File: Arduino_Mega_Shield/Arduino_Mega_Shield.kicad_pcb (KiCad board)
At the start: 4 copper layers, 99.5 x 53.3 mm, 58 parts, among them J1 Conn_01x04, J11 SW6, J12 SW7, J13 SW8, J14 SW9, J15 Motor Driver Connector, J16 Motor Driver Connector, J17 Motor Driver Connector, J18 Motor Driver Connector, J19 Screw_Terminal_01x02, J2 Conn_01x04, J20 JOYSTICK, J21 I2C CONNECTOR, J22 ENCODER1, J23 ENCODER2, J24 ENCODER3, J25 ENCODER4, J26 UART CONNECTOR, J27 3_pin_selector, J28 3_pin_selector, J29 3_pin_selector, J3 Conn_01x04, J30 3_pin_selector, J31 3_pin_selector, J32 3_pin_selector, J33 3_pin_selector, J34 3_pin_selector, J35 3_pin_selector, J36 3_pin_selector, J37 3_pin_selector, J38 3_pin_selector, J39 SW10, J4 Conn_01x04, J5 SW5, J6 SW1, J7 SW2, J8 SW3, J9 SW4

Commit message: Final version of the PCB
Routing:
- net SW8: track 0.00 -> 124.6 mm, vias 0 -> 1
- net SW6: track 0.00 -> 107.0 mm, vias 0 -> 2
- net SW7: track 0.00 -> 104.2 mm, vias 0 -> 2
- net SW5: track 0.00 -> 99.0 mm, vias 0 -> 1
- net SW4: track 0.00 -> 90.1 mm, vias 0 -> 2
- net SW3: track 0.00 -> 81.7 mm, vias 0 -> 1
- net SW2: track 0.00 -> 78.4 mm
- net SW1: track 0.00 -> 71.4 mm, vias 0 -> 1
- net SW9: track 0.00 -> 30.2 mm
- net SW10: track 0.00 -> 25.9 mm, vias 0 -> 1
- net +12V: track 226.7 -> 224.8 mm
- net VRY: track 61.8 -> 60.5 mm
- net R_IS3: track 76.6 -> 77.5 mm
- net ENC_A1: track 16.8 -> 15.9 mm
- net R_IS2: track 52.5 -> 51.8 mm
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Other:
- board text added: "STAR"
- board text added: "TMB"
- board text added: "TRACK"
- board text removed: "Made by Josserand-Pierre Gay with the help of Simon Guillemette"

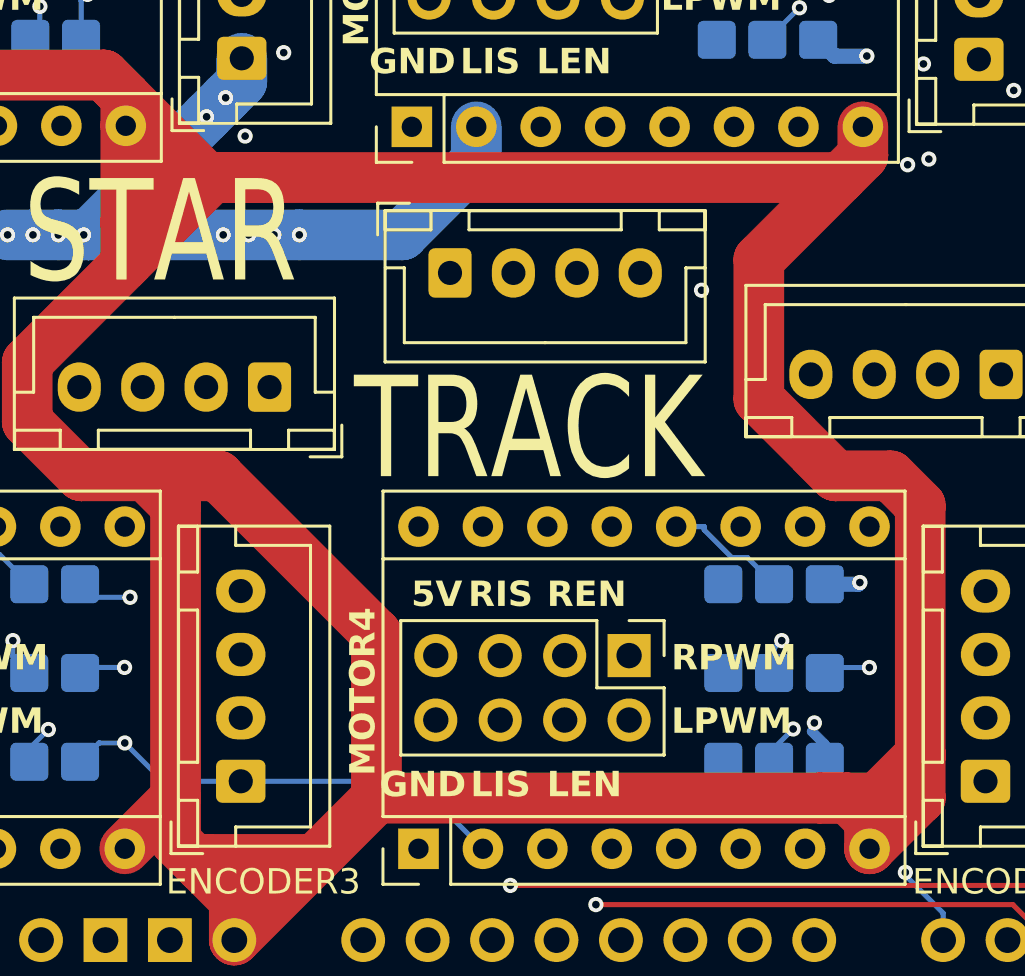
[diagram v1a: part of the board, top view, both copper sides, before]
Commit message: Refactor of the Arduino code to improve readability and debugging
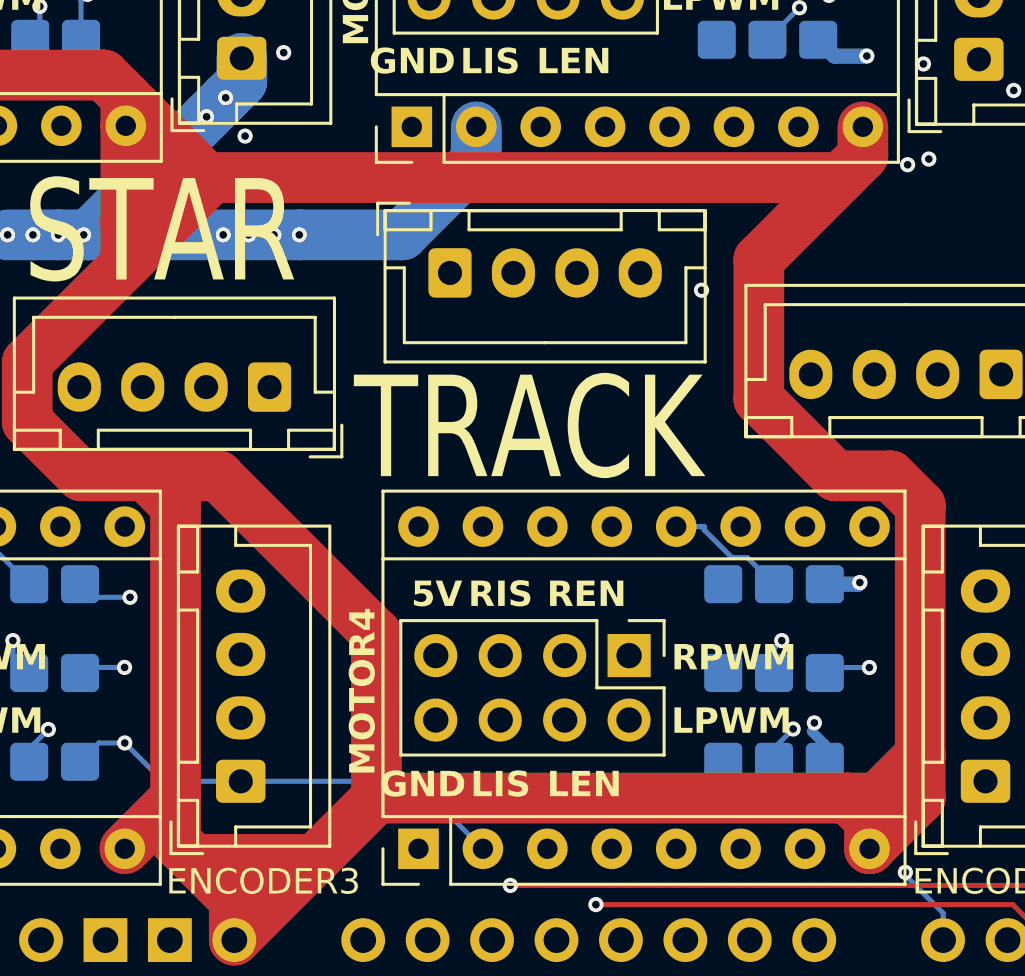
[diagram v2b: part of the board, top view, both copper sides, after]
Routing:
- net +12V: track 224.8 -> 218.1 mm
- net SW6: track 107.0 -> 105.0 mm
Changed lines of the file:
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@@
-	)
-	(segment
-		(start 139 84.241)
-		(end 138.06 84.241)
-		(width 2)
-		(layer "F.Cu")
-		(net 61)
 	)
 	(segment
@@
 	)
 	(segment
-		(start 140.5 84.241)
-		(end 139 84.241)
-		(width 2)
-		(layer "F.Cu")
-		(net 61)
-	)
-	(segment
 		(start 117.735 80.199)
 		(end 133.79 80.199)
@@
 	)
 	(segment
-		(start 137.832 84.241)
-		(end 136.701 84.241)
-		(width 2)
-		(layer "F.Cu")
-		(net 61)
-	)
-	(segment
 		(start 111.999 73.8628)
 		(end 113.939 73.8628)
@@
 	)
 	(segment
-		(start 137.832 84.241)
-		(end 138.06 84.241)
-		(width 2)
-		(layer "F.Cu")
-		(net 61)
-	)
-	(segment
 		(start 133.79 80.199)
 		(end 137.832 84.241)
@@
 	)
 	(segment
-		(start 138.06 84.241)
-		(end 139 84.241)
-		(width 2)
-		(layer "F.Cu")
-		(net 61)
-	)
-	(segment
 		(start 133.79 80.199)
 		(end 134.66 81.0686)
@@
 	)
 	(segment
-		(start 137.832 84.241)
-		(end 138.06 84.241)
-		(width 2)
-		(layer "F.Cu")
-		(net 61)
-	)
-	(segment
 		(start 136.701 84.241)
 		(end 136.419 84.241)
@@
 	)
 	(segment
-		(start 139 84.241)
-		(end 140.5 84.241)
-		(width 2)
-		(layer "F.Cu")
-		(net 61)
-	)
-	(segment
-		(start 139 84.241)
-		(end 140.5 84.241)
-		(width 2)
-		(layer "F.Cu")
-		(net 61)
-	)
-	(segment
 		(start 138.06 84.241)
 		(end 134.66 87.6414)
@@
 	)
 	(segment
-		(start 162 108.699)
-		(end 163.108 108.699)
-		(width 2)
-		(layer "F.Cu")
-		(net 61)
-	)
-	(segment
 		(start 134.66 86)
 		(end 134.66 87.6414)
@@
 	(segment
 		(start 144.539 108.699)
-		(end 162 108.699)
+		(end 163.108 108.699)
 		(width 2)
 		(layer "F.Cu")
@@
 	)
 	(segment
-		(start 140.5 84.241)
+		(start 138.06 84.241)
 		(end 162.846 84.241)
 		(width 2)
@@
 		(start 165.979 107)
 		(end 165.979 108.699)
-		(width 2)
-		(layer "F.Cu")
-		(net 61)
-	)
-	(segment
-		(start 162 108.699)
-		(end 163.108 108.699)
 		(width 2)
 		(layer "F.Cu")
@@
 	)
 	(segment
-		(start 108.0956 108.4837)
-		(end 108.4554 108.8435)
-		(width 0.2)
-		(layer "In1.Cu")
-		(net 75)
-	)
-	(segment
 		(start 102.6672 90.962)
 		(end 100.992 92.6372)
@@
 	)
 	(segment
-		(start 108.4554 108.8435)
-		(end 108.0956 108.4837)
-		(width 0.2)
-		(layer "In1.Cu")
-		(net 75)
-	)
-	(segment
 		(start 105.6111 90.962)
 		(end 102.6672 90.962)
@@
 	)
 	(segment
-		(start 108.4554 108.8435)
-		(end 108.0956 108.4837)
-		(width 0.2)
-		(layer "In2.Cu")
-		(net 75)
-	)
-	(segment
 		(start 108.6189 109.007)
 		(end 135.341 109.007)
@@
 		(start 176.3326 109.6537)
 		(end 178.1914 111.5125)
-		(width 0.2)
-		(layer "In2.Cu")
-		(net 75)
-	)
-	(segment
-		(start 108.0956 108.4837)
-		(end 108.4554 108.8435)
 		(width 0.2)
 		(layer "In2.Cu")
@@
 	)
 	(segment
-		(start 164.607 112.369)
-		(end 164.44 112.536)
-		(width 0.2)
-		(layer "In2.Cu")
-		(net 89)
-	)
-	(segment
 		(start 154.281 112.536)
 		(end 152.803 114.013)
@@
 	)
 	(segment
-		(start 164.607 112.369)
-		(end 164.44 112.536)
-		(width 0.2)
-		(layer "In2.Cu")
-		(net 89)
-	)
-	(segment
-		(start 164.842 112.134)
-		(end 164.607 112.369)
-		(width 0.2)
-		(layer "In2.Cu")
+		(start 164.44 112.536)
+		(end 164.842 112.134)
+		(width 0.2)
+		(layer "In2.Cu")
